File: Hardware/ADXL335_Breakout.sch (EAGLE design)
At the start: 10 parts

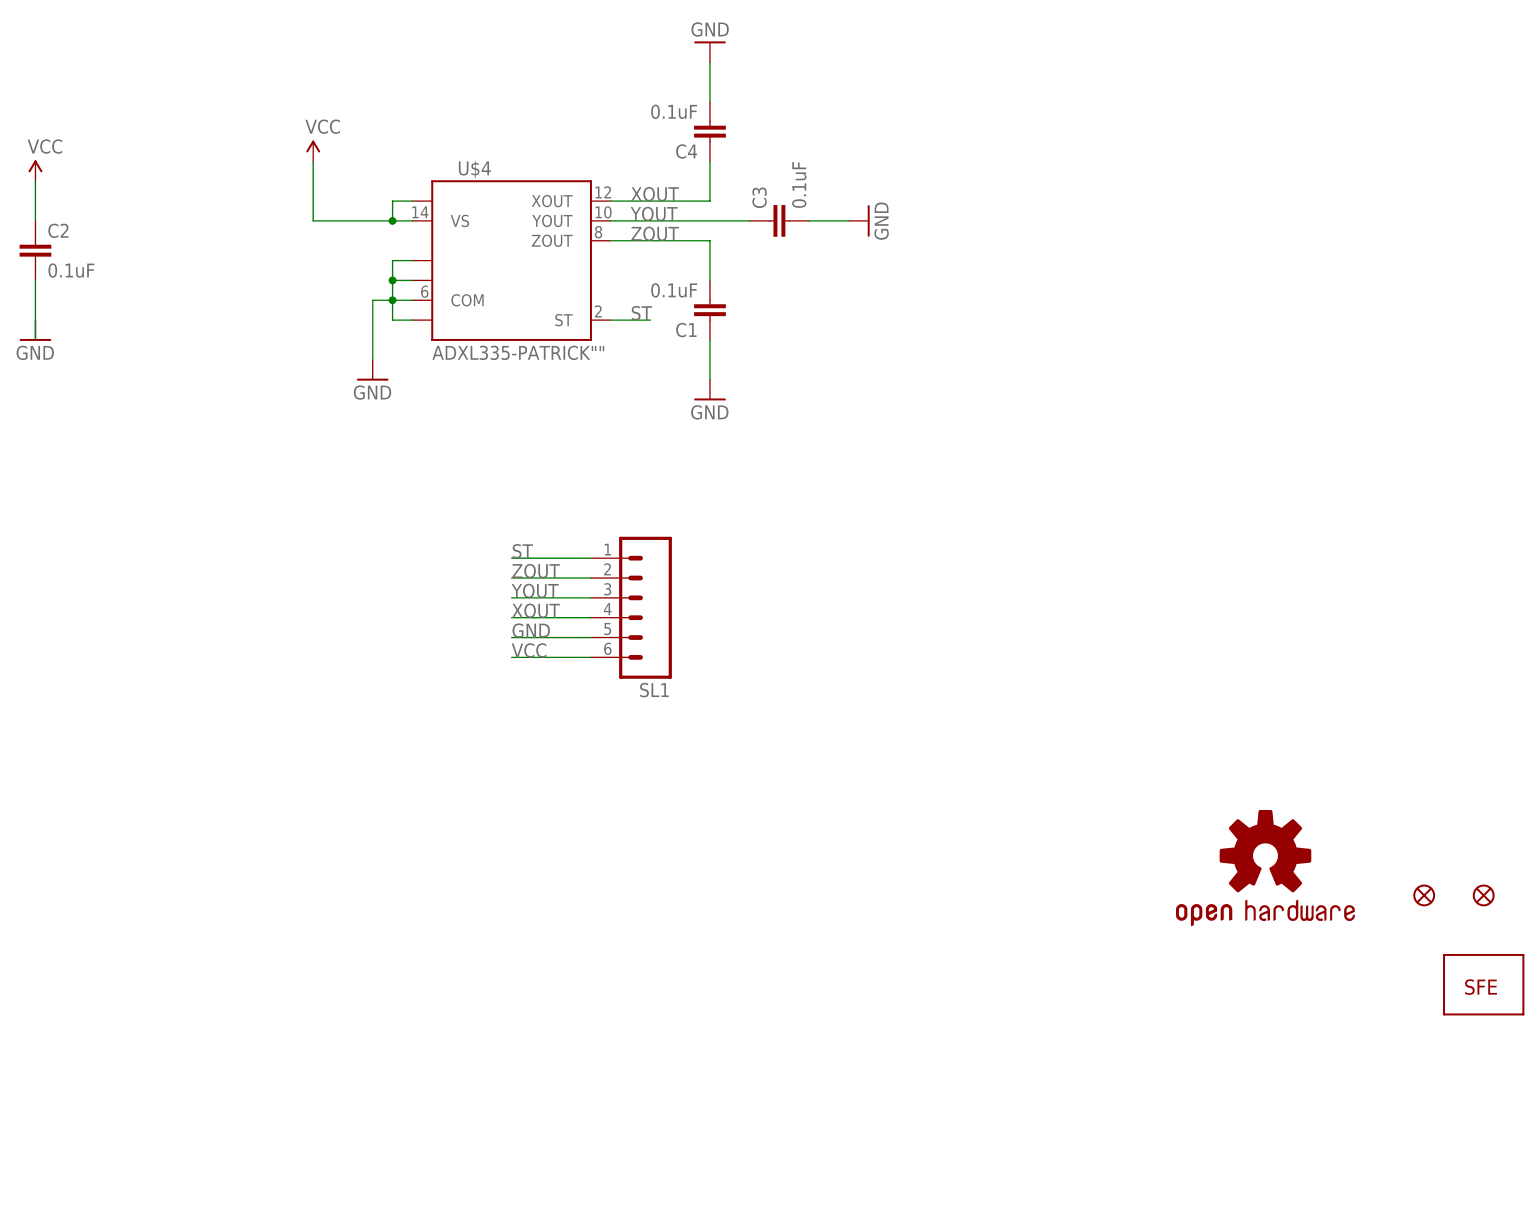
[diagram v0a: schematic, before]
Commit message: Rev Dimension/Silk Design and more
A redo on the dimension of the PCB, Added a new axis to the silk,
revised the bplace with new aesthetics.  Also standoff holes were added.
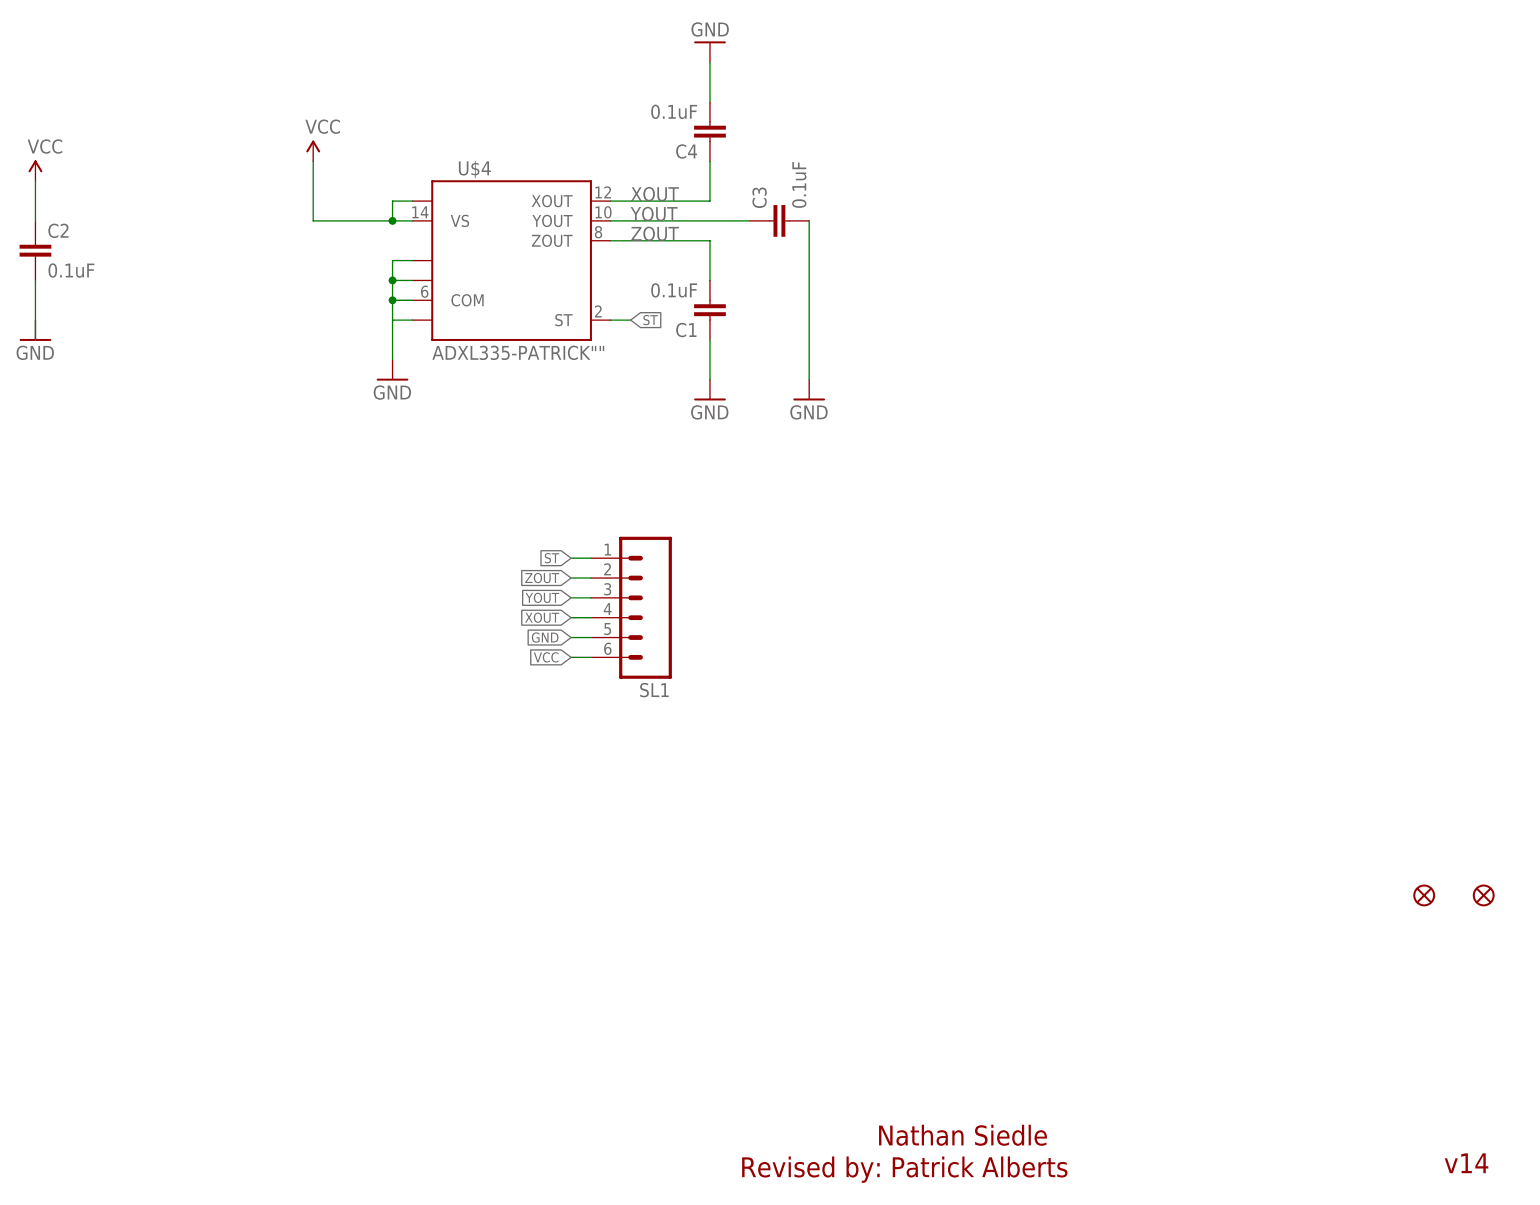
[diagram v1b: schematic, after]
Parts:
- removed U$2: LOGO-SFE, SparkFun:LOGO-SFENEW
- removed U$5: OSHW-LOGOS, SparkFun-Aesthetics:OSHW-LOGOS
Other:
- note added: "Nathan Siedle"
- note added: "Revised by: Patrick Alberts"
- note added: "v14"
